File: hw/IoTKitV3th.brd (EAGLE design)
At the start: 97.5 x 58.4 mm, 28 parts, among them J1 4P-2.0, J2 4P-2.0, J3 4P-2.0, J4 4p-2.54

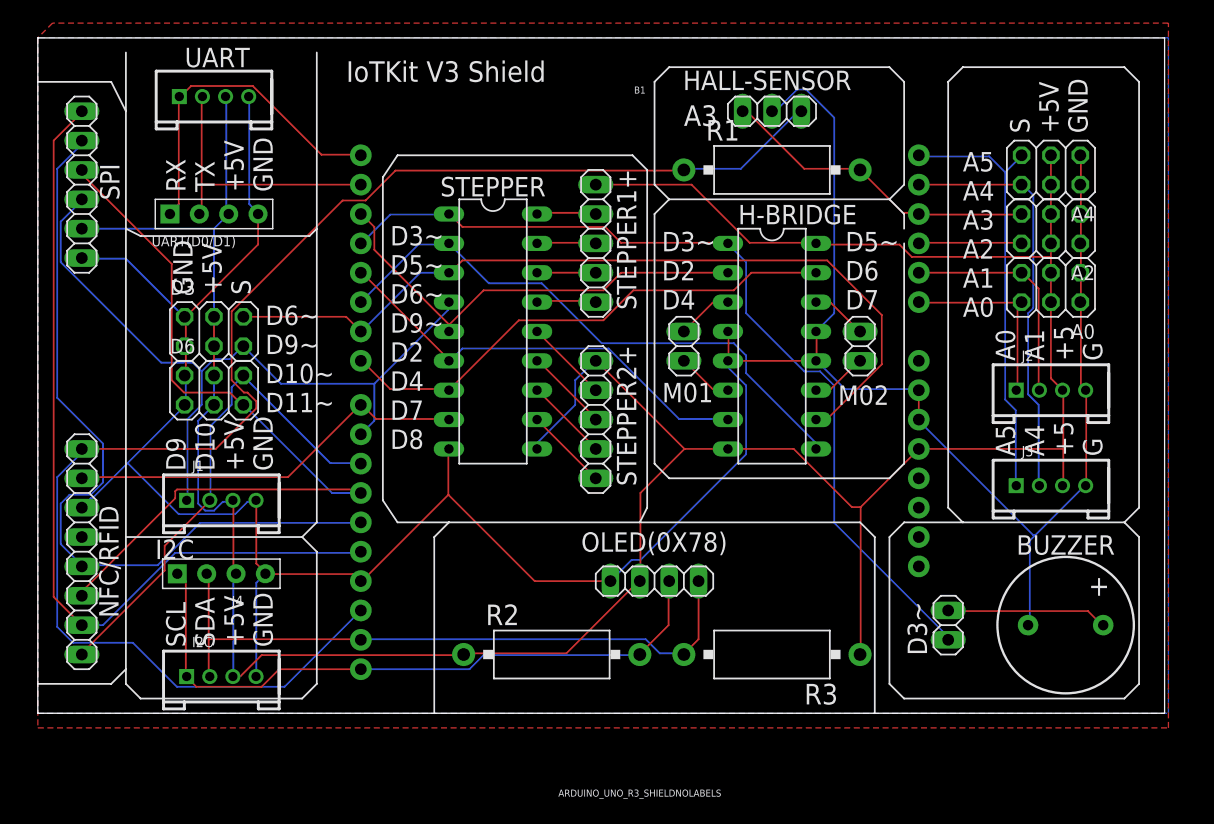
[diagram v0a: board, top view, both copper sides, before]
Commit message: V1.1 inkl. SD Card, Poti, ESP8266, Schrift gekehrt
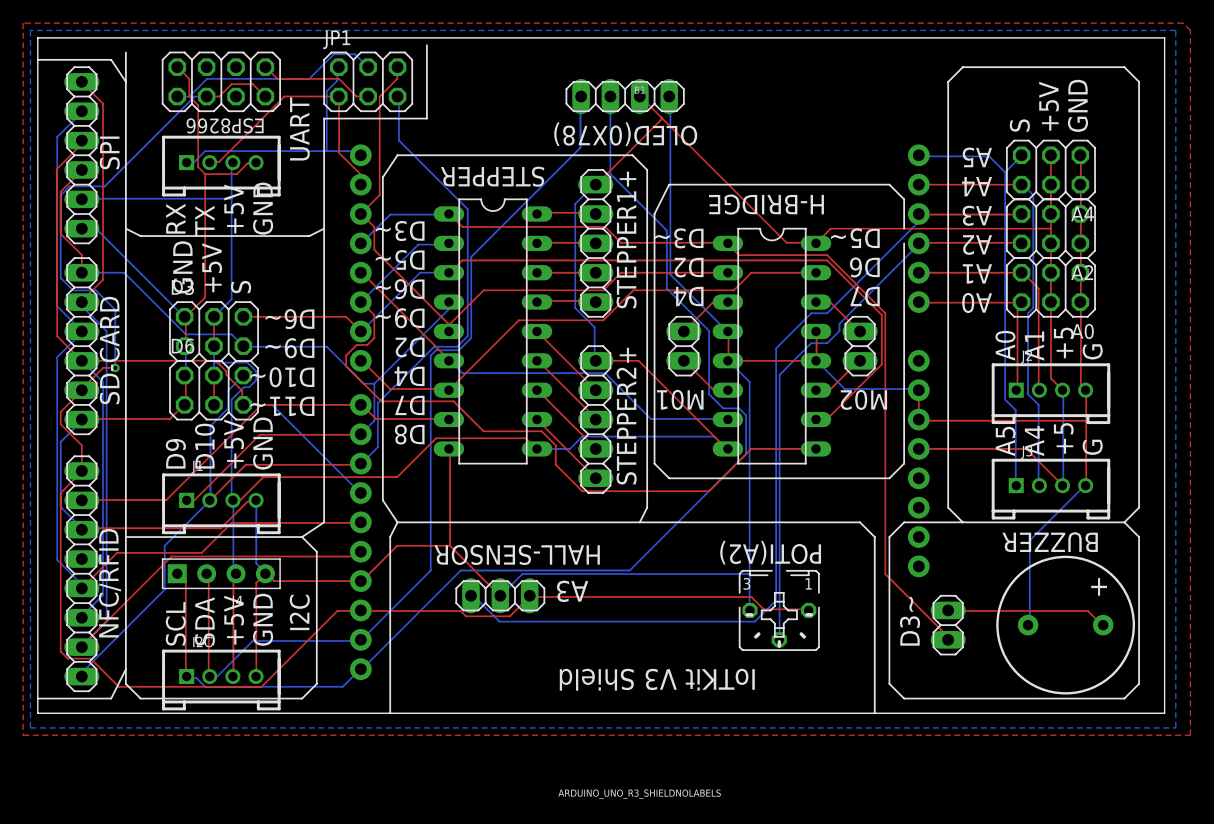
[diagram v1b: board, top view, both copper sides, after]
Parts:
- removed R1: 10k7, resistor-power:CA0001
- removed R2, R3: 4k7, resistor-power:CA0001
- removed UART(D0/D1): UART, Seeed-Connector:H4-2.54
- added ESP8266: (no value), pinhead:2X04
- added JP1: (no value), pinhead:2X03
- added POTI(A2): (no value), pot:B25P
- added SD-CARD: (no value), pinhead:1X06
- moved HALL-SENSOR 48.0 mm to (40.0, 10.2)
- moved OLED(0X78) 42.0 mm to (50.8, 53.3), turned to 180 degrees
- moved UART 5.75 mm to (15.9, 47.6)
- moved SPI 2.54 mm to (3.81, 48.3)
- moved NFC/RFID 1.91 mm to (3.81, 12.1)
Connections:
- new net N$8: ESP8266.1, JP1.3
- new net N$9: ESP8266.8, JP1.4
- net +3V3: now also ESP8266.2, ESP8266.6, POTI(A2).A, SD-CARD.2; no longer R1.1
- net +5V: no longer R2.1, R3.1, UART(D0/D1).3
- net A2: now also POTI(A2).S
- net A3: no longer R1.2
- net D10: now also JP1.5
- net D11: now also SD-CARD.3
- net D12: now also SD-CARD.4
- net D13: now also SD-CARD.5
- net D2: now also JP1.6
- net D9: now also SD-CARD.6
- net GND: now also ESP8266.7, POTI(A2).E, SD-CARD.1; no longer UART(D0/D1).4
- net RX: now also JP1.2; no longer UART(D0/D1).1
- net SCL: no longer R2.2
- net SDA: no longer R3.2
- net TX: now also JP1.1; no longer UART(D0/D1).2
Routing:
- net A3: track 28.0 -> 76.4 mm
- net SCL: track 57.5 -> 103.0 mm
- net D10: track 43.3 -> 85.6 mm
- net A2: track 8.96 -> 49.0 mm
- net GND: track 257.6 -> 283.2 mm
- net +5V: track 260.0 -> 236.5 mm
- net SDA: track 57.6 -> 79.5 mm
- net N$9: track 0.00 -> 18.5 mm
- net D5: track 50.1 -> 65.0 mm
- net D2: track 39.9 -> 53.9 mm
- net N$8: track 0.00 -> 9.94 mm
- net +3V3: track 129.9 -> 139.0 mm, vias 0 -> 1
- net D13: track 73.3 -> 79.8 mm
- net D9: track 65.8 -> 71.7 mm
- net RX: track 29.1 -> 23.3 mm
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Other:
- board text added: "A0 A1 A2 A3 A4 A5"
- board text added: "D11~ D10~ D9~ D6~"
- board text added: "D2 - RX(D0) D10 - TX(D1)"
- board text added: "D4 D2 D3~"
- board text added: "D7 D6 D5~"
- board text added: "D8 D7 D4 D2 D9~ D6~ D5~ D3~"
- board text added: "IoTKit V3, Rev. 1.1, 2019 Designed to work with mbed https://github.com/mc-b/iotkitv3"
- board text added: "SS (D9) SCLK(D13) MOSI(D12) MISO(D11) +3V3 GND"
- board text removed: "A5 A4 A3 A2 A1 A0"
- board text removed: "D3~ D2 D4"
- board text removed: "D3~ D5~ D6~ D9~ D2 D4 D7 D8"
- board text removed: "D5~ D6 D7"
- board text removed: "D6~ D9~ D10~ D11~"
- board text removed: "IoTKit V3, Rev. 1.0, 2018 https://github.com/mc-b/iotkitv3_disco Designed to work with mbed"

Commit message: Korrektur SD Karten belegung
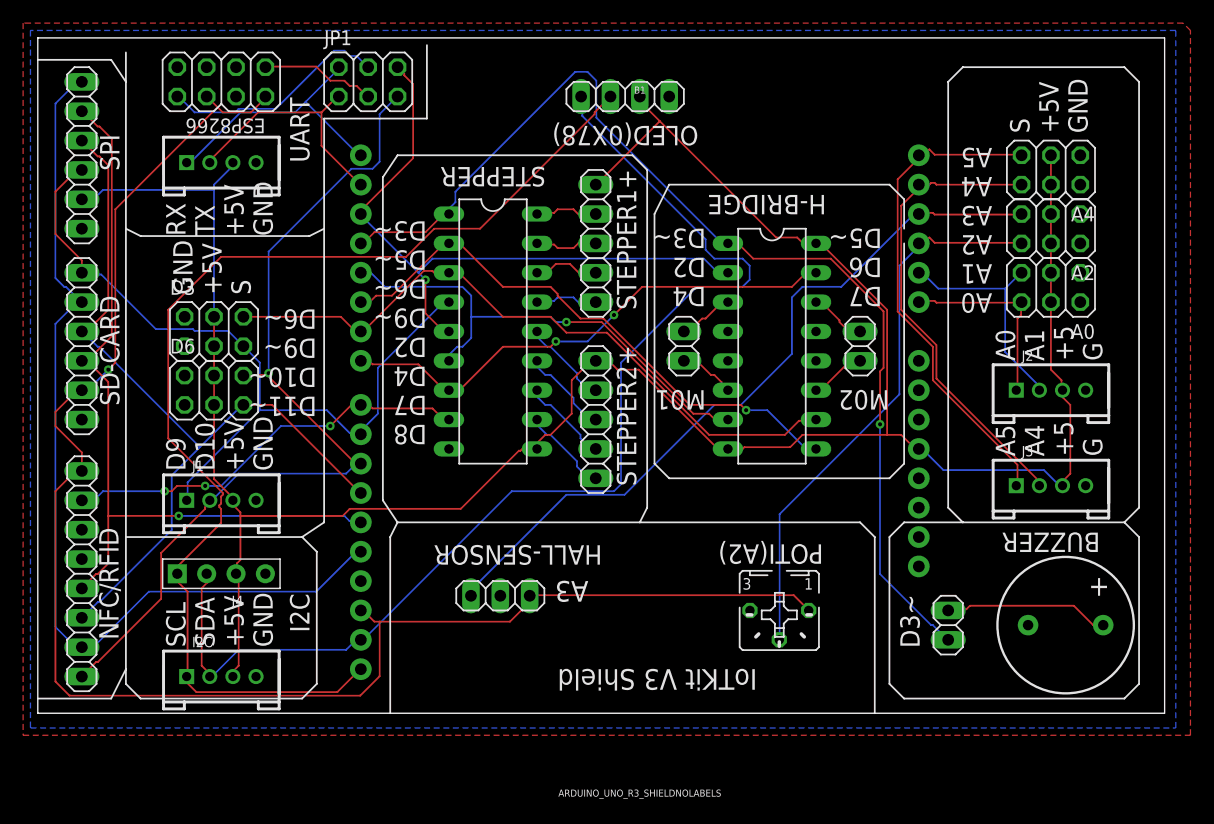
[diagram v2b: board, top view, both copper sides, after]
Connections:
- net D11: now also SD-CARD.4; no longer SD-CARD.3
- net D12: now also SD-CARD.3; no longer SD-CARD.4
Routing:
- net GND: track 283.2 -> 0.00 mm
- net SDA: track 79.5 -> 100.0 mm
- net +5V: track 236.5 -> 220.1 mm
- net D5: track 65.0 -> 48.9 mm, vias 0 -> 1
- net D6: track 72.2 -> 58.7 mm
- net D3: track 80.5 -> 93.8 mm, vias 0 -> 1
- net A3: track 76.4 -> 64.7 mm
- net D10: track 85.6 -> 77.6 mm, vias 0 -> 1
- net D4: track 37.2 -> 43.0 mm, vias 0 -> 1
- net A5: track 37.7 -> 43.0 mm
- net A4: track 36.0 -> 40.6 mm
- net SCL: track 103.0 -> 98.6 mm
- net D12: track 71.3 -> 67.8 mm, vias 0 -> 1
- net D11: track 74.3 -> 70.9 mm
- net D9: track 71.7 -> 68.7 mm
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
